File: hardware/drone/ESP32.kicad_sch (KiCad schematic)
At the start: 23 parts, among them J103 Conn_01x05_Pin, U102 ESP32-S3, Y101 FH4000074Z

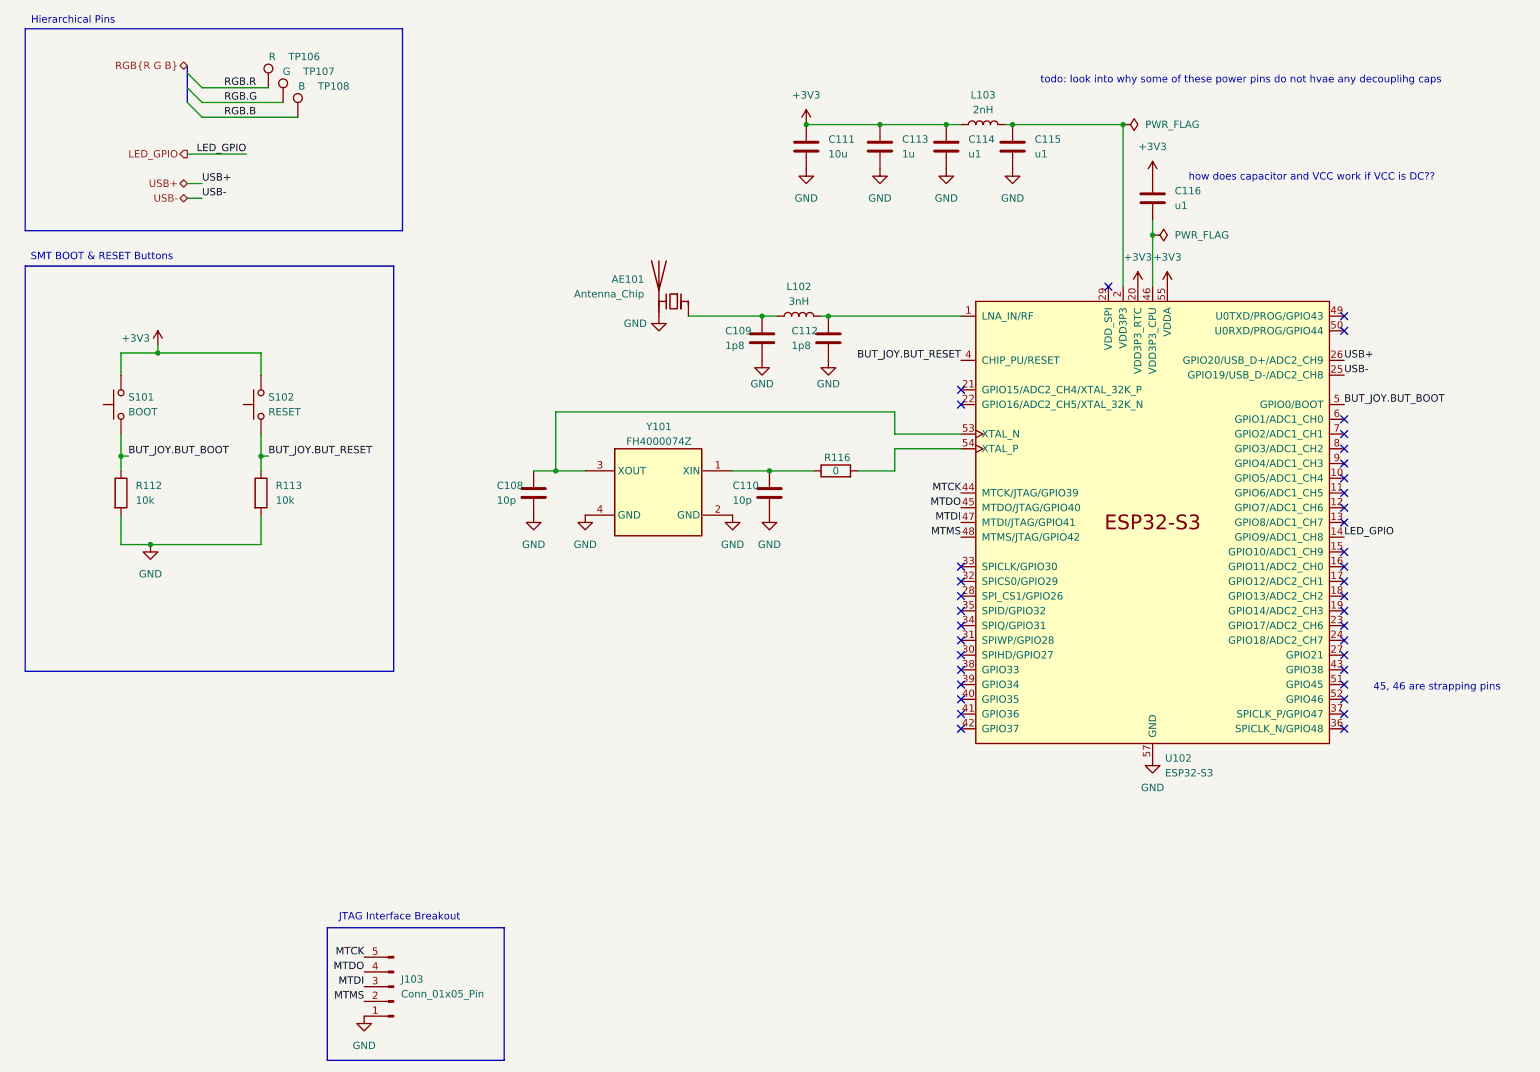
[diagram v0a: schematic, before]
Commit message: save before axing motor driver ic's
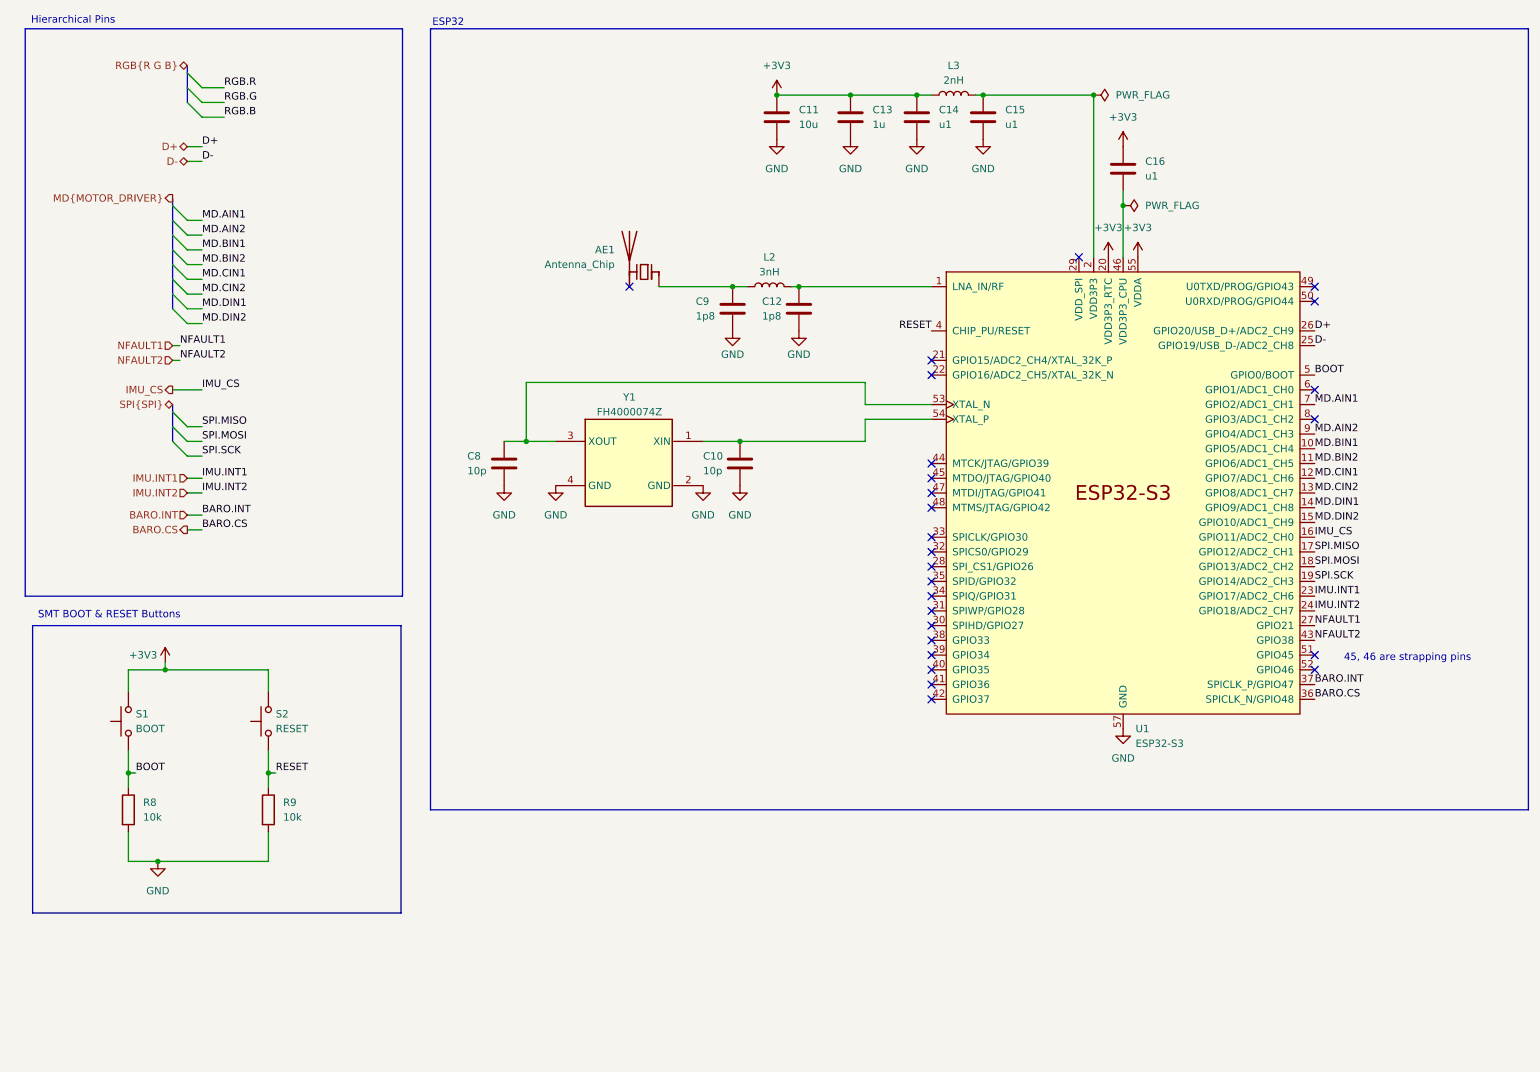
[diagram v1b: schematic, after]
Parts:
- removed J103: Conn_01x05_Pin, Connector_PinHeader_2.54mm:PinHeader_1x05_P2.54mm_Vertical, symbol Connector:Conn_01x05_Pin
- removed R116: 0, SamacSys_Parts:RESC1608X50N, symbol Device:R
- removed TP106: R, TestPoint:TestPoint_Pad_1.0x1.0mm, symbol Connector:TestPoint
- removed TP107: G, TestPoint:TestPoint_Pad_1.0x1.0mm, symbol Connector:TestPoint
- removed TP108: B, TestPoint:TestPoint_Pad_1.0x1.0mm, symbol Connector:TestPoint
- AE1: renamed from AE101; footprint SamacSys_Parts:Texas_SWRA117D_2.4GHz_Left -> SamacSys_Parts:AANI-CH-0133; Mouser Price/Stock (none) -> https://www.mouser.com/ProductDetail/ABRACON/AANI-CH-0133-T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
- C12: renamed from C112; Mouser Price/Stock https://www.mouser.com/ProductDetail/KYOCERA-AVX/KGQ15ACG2A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 -> https://www.mouser.co.uk/ProductDetail/KYOCERA-AVX/KGQ15ACG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
- C9: renamed from C109; Mouser Price/Stock https://www.mouser.com/ProductDetail/KYOCERA-AVX/KGQ15ACG2A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 -> https://www.mouser.co.uk/ProductDetail/KYOCERA-AVX/KGQ15ACG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
- renumbered C110 to C10, C111 to C11, C113 to C13, C114 to C14, C115 to C15, C116 to C16, C108 to C8, L102 to L2, L103 to L3, R112 to R8, R113 to R9, S101 to S1, S102 to S2, U102 to U1, Y101 to Y1
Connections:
- net GND: no longer AE1.2 (PCB_Trace)
- net at C10.1, Y1.1 (XIN): now also U1.54 (XTAL_P)
- net MD.BIN1: now reaches U1.10 (GPIO5/ADC1_CH4)
- net MD.BIN2: now reaches U1.11 (GPIO6/ADC1_CH5)
- net MD.CIN1: now reaches U1.12 (GPIO7/ADC1_CH6)
- net MD.CIN2: now reaches U1.13 (GPIO8/ADC1_CH7)
- net MD.DIN2: now reaches U1.15 (GPIO10/ADC1_CH9)
- net IMU_CS: now reaches U1.16 (GPIO11/ADC2_CH0)
- net SPI.MISO: now reaches U1.17 (GPIO12/ADC2_CH1)
- net SPI.MOSI: now reaches U1.18 (GPIO13/ADC2_CH2)
- net SPI.SCK: now reaches U1.19 (GPIO14/ADC2_CH3)
- net IMU.INT1: now reaches U1.23 (GPIO17/ADC2_CH6)
- net IMU.INT2: now reaches U1.24 (GPIO18/ADC2_CH7)
- net NFAULT1: now reaches U1.27 (GPIO21)
- net BARO.CS: now reaches U1.36 (SPICLK_N/GPIO48)
- net BARO.INT: now reaches U1.37 (SPICLK_P/GPIO47)
- net NFAULT2: now reaches U1.43 (GPIO38)
- net MD.AIN1: now reaches U1.7 (GPIO2/ADC1_CH1)
- net MD.AIN2: now reaches U1.9 (GPIO4/ADC1_CH3)
- net BUT_JOY.BUT_BOOT renamed BOOT
- net BUT_JOY.BUT_RESET renamed RESET
- net LED_GPIO renamed MD.DIN1
- net MTCK: no longer names the net of U1.44 (MTCK/JTAG/GPIO39)
- net MTDI: no longer names the net of U1.47 (MTDI/JTAG/GPIO41)
- net MTDO: no longer names the net of U1.45 (MTDO/JTAG/GPIO40)
- net MTMS: no longer names the net of U1.48 (MTMS/JTAG/GPIO42)
- net USB+ renamed D+
- net USB- renamed D-
- no-connect marks 38 -> 26
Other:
- note added: "ESP32"
- note removed: "JTAG Interface Breakout"
- note removed: "how does capacitor and VCC work if VCC is DC??"
- note removed: "todo: look into why some of these power pins do not hvae any decouplihg caps"
- moved on the sheet: AE1, C10, C11, C12, C13, C14, C15, C16, C8, C9, L2, L3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

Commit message: axed motor drivers. finished layout for drone but need to review overall system design after reading some stuff
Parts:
- renumbered R8 to R10, R9 to R11
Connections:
- net +3V3: now also U1.46 (VDD3P3_CPU)
- net GND: now also C16.2
- net RGB.B: now also U1.41 (GPIO36)
- net RGB.G: now also U1.40 (GPIO35)
- net RGB.R: now also U1.39 (GPIO34)
- net MOTORS.MA: now reaches U1.6 (GPIO1/ADC1_CH0)
- net MOTORS.MC: now reaches U1.8 (GPIO3/ADC1_CH2)
- net MD.AIN1 renamed MOTORS.MB
- net MD.AIN2 renamed MOTORS.MD
- net MD.BIN1: no longer names the net of U1.10 (GPIO5/ADC1_CH4)
- net MD.BIN2: no longer names the net of U1.11 (GPIO6/ADC1_CH5)
- net MD.CIN1: no longer names the net of U1.12 (GPIO7/ADC1_CH6)
- net MD.CIN2: no longer names the net of U1.13 (GPIO8/ADC1_CH7)
- net MD.DIN1: no longer names the net of U1.14 (GPIO9/ADC1_CH8)
- net MD.DIN2: no longer names the net of U1.15 (GPIO10/ADC1_CH9)
- net NFAULT1: no longer names the net of U1.27 (GPIO21)
- net NFAULT2: no longer names the net of U1.43 (GPIO38)
- no-connect marks 26 -> 29
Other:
- moved on the sheet: C16
